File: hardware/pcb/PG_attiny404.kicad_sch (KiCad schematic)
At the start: 28 parts, among them J1 0022232041, J2 Conn_01x01_Male, J3 Conn_01x01_Male, J4 Conn_01x01_Male, J5 Conn_01x01_Male, J6 Conn_01x01_Male, J7 Conn_01x01_Male, J8 Conn_01x01_Male, Q1 2N7002, SW1 SW_Push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

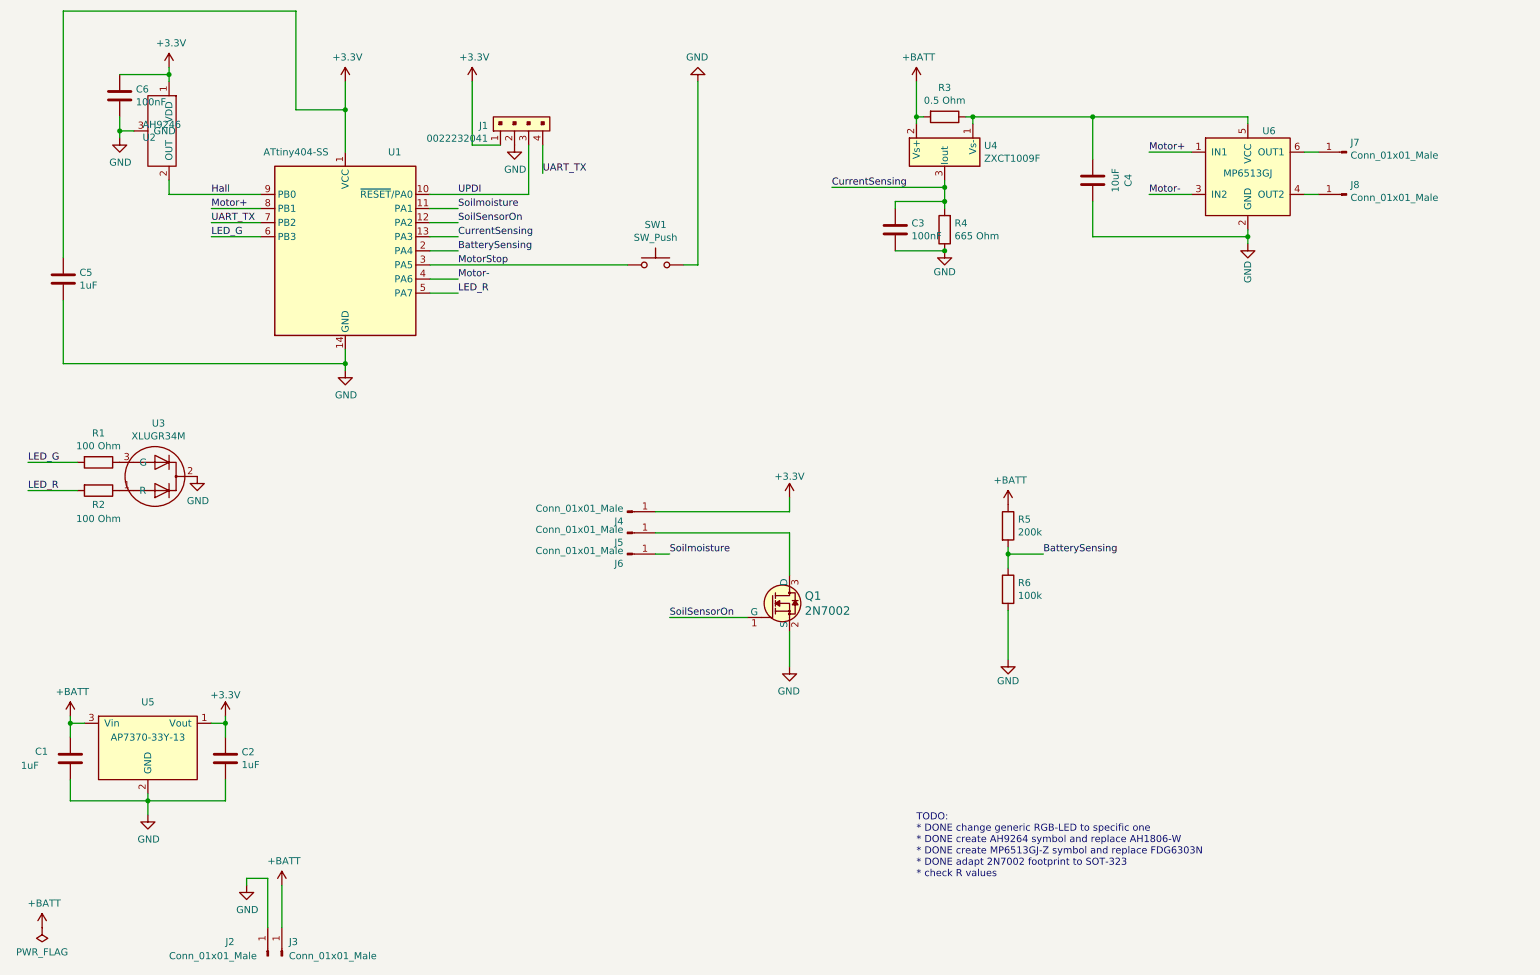
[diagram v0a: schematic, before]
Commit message: Equiped PCB with additional led, changed other led, changed position of solder pads and side of hall sensor
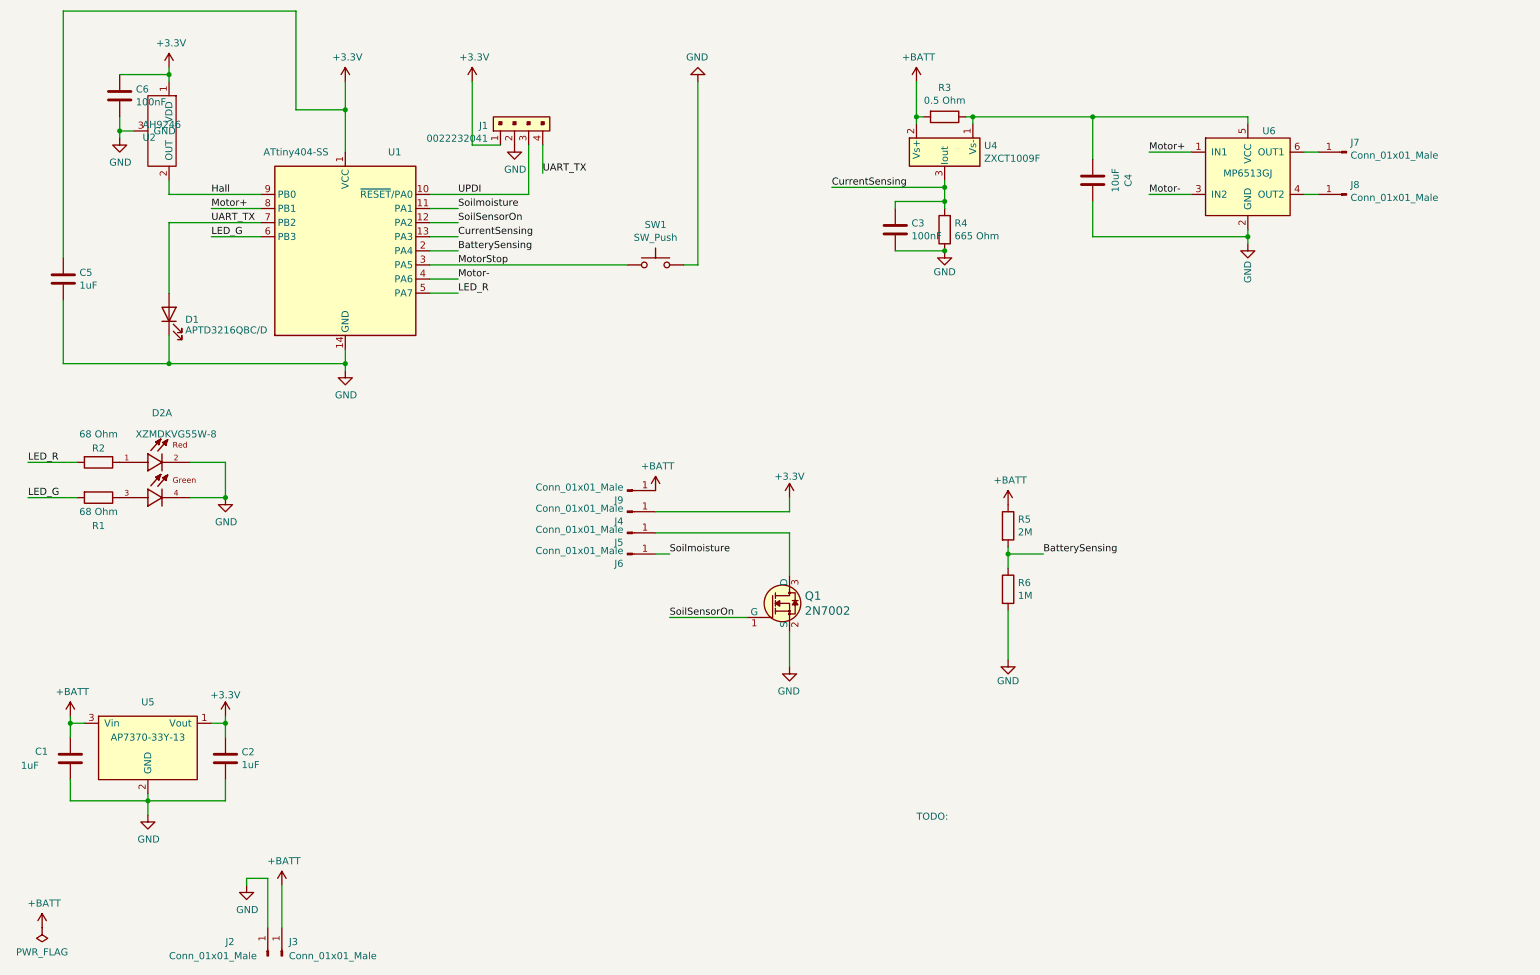
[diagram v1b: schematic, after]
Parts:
- removed U3: XLUGR34M, LED_THT:LED_D3.0mm-3, symbol project:XLUGR34M
- added D1: APTD3216QBC/D, LED_SMD:LED_1206_3216Metric_Pad1.42x1.75mm_HandSolder, symbol Device:LED
- added D2: XZMDKVG55W-8, XZMDKVG55W-8:LED_XZMDKVG55W-8, symbol XZMDKVG55W-8:XZMDKVG55W-8
- added J9: Conn_01x01_Male, digikey-footprints:PROBE_PAD_1206, symbol Connector:Conn_01x01_Male
- C1, C2, C4, C5: DK_Detail_Page (none) -> https://www.digikey.at/de/products/detail/samsung-electro-m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
- C3, C6: DK_Detail_Page (none) -> https://www.digikey.at/de/products/detail/yageo/CC0805KRX7R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
- J1: footprint Connector_PinSocket_2.54mm:PinSocket_1x04_P2.54mm_Horizontal -> Connector_PinHeader_2.54mm:PinHeader_1x04_P2.54mm_Horizontal; DK_Detail_Page /product-detail/en/molex/0022232041/WM4202-ND/26671 -> https://www.digikey.at/de/products/detail/amphenol-cs-fci/8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
- Q1: DK_Detail_Page /product-detail/en/on-semiconductor/2N7002/2N7002NCT-ND/244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 -> https://www.digikey.at/de/products/detail/panjit-internatio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
- R1, R2: value 100 Ohm -> 68 Ohm; DK_Detail_Page (none) -> https://www.digikey.at/de/products/detail/bourns-inc/CR0805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
- R3: DK_Detail_Page (none) -> https://www.digikey.at/de/products/detail/susumu/RL1220S-R5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
- R4: DK_Detail_Page (none) -> https://www.digikey.at/de/products/detail/te-connectivity-p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
- R5: value 200k -> 2M
- R6: value 100k -> 1M
- SW1: DK_Detail_Page (none) -> https://www.digikey.at/de/products/detail/te-connectivity-a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
- U1: DK_Detail_Page (none) -> https://www.digikey.at/de/products/detail/microchip-technol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
- U2, U4, U5: DK_Detail_Page (none) -> https://www.digikey.at/de/products/detail/diodes-incorporat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
- U6: DK_Detail_Page (none) -> https://www.digikey.at/en/products/detail/monolithic-power-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
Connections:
- net +BATT: now also J9.1 (Pin_1)
- net GND: now also D1.1 (K), D2.2, D2.4
- net UART_TX: now also D1.2 (A)
- net at R1.1: now also D2.3
- net at R2.1: now also D2.1
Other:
- note added: "TODO:"
- note removed: "TODO: * DONE change generic RGB-LED to specific one * DONE create AH9264 symbol and replace AH1806-W * DONE create MP6513GJ-Z symbol and replace FDG6303N * DONE adapt 2N7002 footprint to SOT-323 * check R values"
- moved on the sheet: R1, R2

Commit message: Added Interactive Bom
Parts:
- J1: DK_Detail_Page https://www.digikey.at/de/products/detail/amphenol-cs-fci/8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 -> https://www.digikey.at/de/products/detail/molex/0022286040/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
- R1, R2: DK_Detail_Page https://www.digikey.at/de/products/detail/bourns-inc/CR0805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 -> https://www.digikey.at/de/products/detail/stackpole-electro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
- R5, R6: DK_Detail_Page (none) -> https://www.digikey.at/de/products/detail/stackpole-electro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
- U1: DK_Detail_Page https://www.digikey.at/de/products/detail/microchip-technology/ATTINY404-SSNR/8594960 -> https://www.digikey.at/de/products/detail/microchip-technology/ATTINY804-SSNR/10270299
- U6: DK_Detail_Page https://www.digikey.at/en/products/detail/monolithic-power-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 -> https://www.digikey.at/de/products/detail/monolithic-power-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
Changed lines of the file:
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@@
       (effects (font (size 1.27 1.27)) hide)
     )
-    (property "DK_Detail_Page" "https://www.digikey.at/de/products/detail/microchip-technology/ATTINY404-SSNR/8594960 " (at 76.2 66.04 0)
+    (property "DK_Detail_Page" "https://www.digikey.at/de/products/detail/microchip-technology/ATTINY804-SSNR/10270299" (at 76.2 66.04 0)
       (effects (font (size 1.27 1.27)) hide)
     )
@@
       (effects (font (size 1.27 1.27)) hide)
     )
-    (property "DK_Detail_Page" "https://www.digikey.at/de/products/detail/bourns-inc/CR0805-JW-101ELF/3741029 " (at 31.75 110.49 0)
+    (property "DK_Detail_Page" "https://www.digikey.at/de/products/detail/stackpole-electronics-inc/RMCF0805FT68R0/1713312" (at 31.75 110.49 0)
       (effects (font (size 1.27 1.27)) hide)
     )
@@
       (effects (font (size 1.27 1.27)) hide)
     )
-    (property "DK_Detail_Page" "https://www.digikey.at/de/products/detail/bourns-inc/CR0805-JW-101ELF/3741029 " (at 31.75 104.14 0)
+    (property "DK_Detail_Page" "https://www.digikey.at/de/products/detail/stackpole-electronics-inc/RMCF0805FT68R0/1713312" (at 31.75 104.14 0)
       (effects (font (size 1.27 1.27)) hide)
     )
@@
       (effects (font (size 1.27 1.27)) hide)
     )
+    (property "DK_Detail_Page" "https://www.digikey.at/de/products/detail/stackpole-electronics-inc/RMCF0805FT2M00/1760219" (at 195.58 115.57 0)
+      (effects (font (size 1.27 1.27)) hide)
+    )
     (pin "1")
     (pin "2")
@@
       (effects (font (size 1.27 1.27)) hide)
     )
+    (property "DK_Detail_Page" "https://www.digikey.at/de/products/detail/stackpole-electronics-inc/RMCF0805FG1M00/1712780" (at 195.58 127 0)
+      (effects (font (size 1.27 1.27)) hide)
+    )
     (pin "1")
     (pin "2")
@@
       (effects (font (size 1.524 1.524)) (justify left) hide)
     )
-    (property "DK_Detail_Page" "https://www.digikey.at/de/products/detail/amphenol-cs-fci/861400041LO1705LF/4414079 " (at 109.22 67.31 0)
+    (property "DK_Detail_Page" "https://www.digikey.at/de/products/detail/molex/0022286040/3158671" (at 109.22 67.31 0)
       (effects (font (size 1.524 1.524)) (justify left) hide)
     )
@@
       (effects (font (size 1.27 1.27)) hide)
     )
-    (property "DK_Detail_Page" "https://www.digikey.at/en/products/detail/monolithic-power-systems-inc/MP6513GJ-Z/7361427 " (at 238.76 50.8 0)
-      (effects (font (size 1.27 1.27)) hide)
-    )
+    (property "DK_Detail_Page" "https://www.digikey.at/de/products/detail/monolithic-power-systems-inc/MP6513GJ-Z/7361427" (at 238.76 50.8 0)
+      (effects (font (size 1.27 1.27)) hide)
+    )
